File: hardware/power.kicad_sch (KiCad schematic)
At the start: 12 parts, among them J18 Power, SW7 POWER, U14 NCP1117-5.0_SOT223, U15 B0505S-1WR3

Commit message: Reset references and remove THT footprint assignments.
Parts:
- removed J18: Power, Connector_BarrelJack:BarrelJack_Horizontal, symbol Connector:Barrel_Jack_Switch
- added J19: DC, symbol Connector_Generic:Conn_01x03
- D8: footprint Diode_THT:D_DO-41_SOD81_P2.54mm_Vertical_AnodeUp -> (none)
- renumbered R64 to R70, SW7 to SW6
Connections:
- net GND: now also J19.3 (Pin_3)
- net at SW6.1 (A): now also J19.1 (Pin_1)
- net at BT1.1 (+): now also J19.2 (Pin_2)
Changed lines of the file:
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@@
-	)
-	(symbol
-		(lib_id "Connector:Barrel_Jack_Switch")
-		(at 35.56 91.44 0)
-		(mirror x)
-		(unit 1)
-		(exclude_from_sim no)
-		(in_bom yes)
-		(on_board yes)
-		(dnp no)
-		(property "Reference" "J18"
-			(at 35.56 82.55 0)
-			(effects
-				(font
-					(size 1.27 1.27)
-				)
-			)
-		)
-		(property "Value" "Power"
-			(at 35.56 85.0869 0)
-			(effects
-				(font
-					(size 1.27 1.27)
-				)
-			)
-		)
-		(property "Footprint" "Connector_BarrelJack:BarrelJack_Horizontal"
-			(at 36.83 90.424 0)
-			(effects
-				(font
-					(size 1.27 1.27)
-				)
-				(hide yes)
-			)
-		)
-		(property "Datasheet" "~"
-			(at 36.83 90.424 0)
-			(effects
-				(font
-					(size 1.27 1.27)
-				)
-				(hide yes)
-			)
-		)
-		(property "Description" "DC Barrel Jack with an internal switch"
-			(at 35.56 91.44 0)
-			(effects
-				(font
-					(size 1.27 1.27)
-				)
-				(hide yes)
-			)
-		)
-		(pin "1"
-		)
-		(pin "2"
-		)
-		(pin "3"
-		)
-		(instances
-			(project "Zero-Stomp"
-				(path "/8c8d5801-9c58-4283-98ac-c6a8e7250e15/19d3dfe6-4a06-4dc4-92a9-6134eae12961"
-					(reference "J18")
-					(unit 1)
-				)
-			)
-		)
 	)
 	(symbol
@@
 		(dnp no)
 		(fields_autoplaced yes)
-		(property "Reference" "SW7"
+		(property "Reference" "SW6"
 			(at 64.77 82.55 0)
 			(effects
@@
 			(project ""
 				(path "/8c8d5801-9c58-4283-98ac-c6a8e7250e15/19d3dfe6-4a06-4dc4-92a9-6134eae12961"
-					(reference "SW7")
+					(reference "SW6")
 					(unit 1)
 				)
@@
 		(on_board yes)
 		(dnp no)
-		(property "Reference" "R64"
+		(property "Reference" "R70"
 			(at 147.32 92.71 90)
 			(effects
@@
 			(project "Zero-Stomp"
 				(path "/8c8d5801-9c58-4283-98ac-c6a8e7250e15/19d3dfe6-4a06-4dc4-92a9-6134eae12961"
-					(reference "R64")
+					(reference "R70")
 					(unit 1)
 				)
@@
 			)
 		)
-		(property "Footprint" "Diode_THT:D_DO-41_SOD81_P2.54mm_Vertical_AnodeUp"
+		(property "Footprint" ""
 			(at 138.43 81.915 0)
 			(effects
@@
 					(unit 1)
 				)
+			)
+		)
+	)
+	(symbol
+		(lib_id "Connector_Generic:Conn_01x03")
+		(at 38.1 91.44 0)
+		(mirror y)
+		(unit 1)
+		(exclude_from_sim no)
+		(in_bom yes)
+		(on_board yes)
+		(dnp no)
+		(fields_autoplaced yes)
+		(property "Reference" "J19"
+			(at 38.1 82.55 0)
+			(effects
+				(font
+					(size 1.27 1.27)
+				)
+			)
+		)
+		(property "Value" "DC"
+			(at 38.1 85.09 0)
+			(effects
+				(font
+					(size 1.27 1.27)
+				)
+			)
+		)
+		(property "Footprint" ""
+			(at 38.1 91.44 0)
+			(effects
+				(font
+					(size 1.27 1.27)
+				)
+				(hide yes)
+			)
+		)
+		(property "Datasheet" "~"
+			(at 38.1 91.44 0)
+			(effects
+				(font
+					(size 1.27 1.27)
+				)
+				(hide yes)
+			)
+		)
+		(property "Description" "Generic connector, single row, 01x03, script generated (kicad-library-utils/schlib/autogen/connector/)"
+			(at 38.1 91.44 0)
+			(effects
+				(font
+					(size 1.27 1.27)
+				)
+				(hide yes)
+			)
+		)
+		(pin "1"
+		)
+		(pin "3"
+		)
+		(pin "2"
+		)
+		(instances
+			(project ""
+				(path "/8c8d5801-9c58-4283-98ac-c6a8e7250e15/19d3dfe6-4a06-4dc4-92a9-6134eae12961"
+					(reference "J19")
+					(unit 1)
+				)

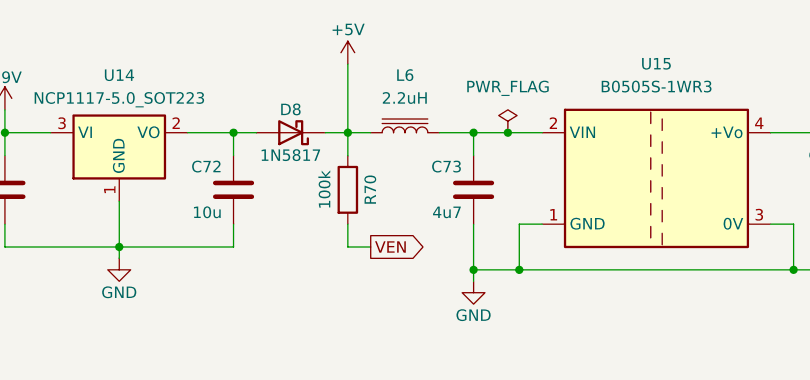
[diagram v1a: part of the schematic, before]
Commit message: Footprint assignments
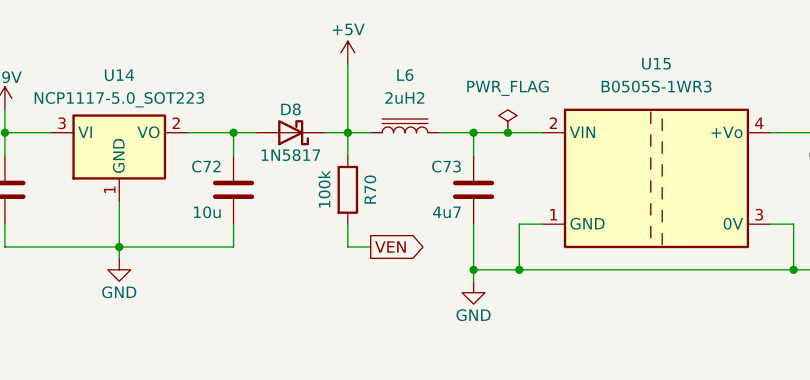
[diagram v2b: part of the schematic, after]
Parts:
- C71, C72, C74: footprint (none) -> Capacitor_SMD:C_0805_2012Metric
- C73: footprint (none) -> Capacitor_SMD:C_0603_1608Metric
- D8: footprint (none) -> Diode_SMD:D_SOD-123
- J19: footprint (none) -> Connector_JST:JST_PH_B3B-PH-K_1x03_P2.00mm_Vertical
- L6: value 2.2uH -> 2uH2; footprint (none) -> Inductor_SMD:L_12x12mm_H4.5mm
- R70: footprint (none) -> Resistor_SMD:R_0603_1608Metric
- SW6: footprint (none) -> Connector_JST:JST_PH_B2B-PH-K_1x02_P2.00mm_Vertical
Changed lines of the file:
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@@
 			)
 		)
-		(property "Footprint" ""
+		(property "Footprint" "Capacitor_SMD:C_0805_2012Metric"
 			(at 131.1148 96.52 0)
 			(effects
@@
 			)
 		)
-		(property "Footprint" ""
+		(property "Footprint" "Connector_JST:JST_PH_B2B-PH-K_1x02_P2.00mm_Vertical"
 			(at 64.77 88.9 0)
 			(effects
@@
 			)
 		)
-		(property "Footprint" ""
+		(property "Footprint" "Resistor_SMD:R_0603_1608Metric"
 			(at 143.002 92.71 90)
 			(effects
@@
 			)
 		)
-		(property "Footprint" ""
+		(property "Footprint" "Capacitor_SMD:C_0603_1608Metric"
 			(at 157.7848 96.52 0)
 			(effects
@@
 			)
 		)
-		(property "Value" "2.2uH"
+		(property "Value" "2uH2"
 			(at 151.13 82.55 90)
 			(effects
@@
 			)
 		)
-		(property "Footprint" ""
+		(property "Footprint" "Inductor_SMD:L_12x12mm_H4.5mm"
 			(at 151.13 86.36 0)
 			(effects
@@
 			)
 		)
-		(property "Footprint" ""
+		(property "Footprint" "Capacitor_SMD:C_0805_2012Metric"
 			(at 199.6948 95.25 0)
 			(effects
@@
 			)
 		)
-		(property "Footprint" ""
+		(property "Footprint" "Diode_SMD:D_SOD-123"
 			(at 138.43 81.915 0)
 			(effects
@@
 			)
 		)
-		(property "Footprint" ""
+		(property "Footprint" "Capacitor_SMD:C_0805_2012Metric"
 			(at 105.7148 96.52 0)
 			(effects
@@
 			)
 		)
-		(property "Footprint" ""
+		(property "Footprint" "Connector_JST:JST_PH_B3B-PH-K_1x03_P2.00mm_Vertical"
 			(at 38.1 91.44 0)
 			(effects

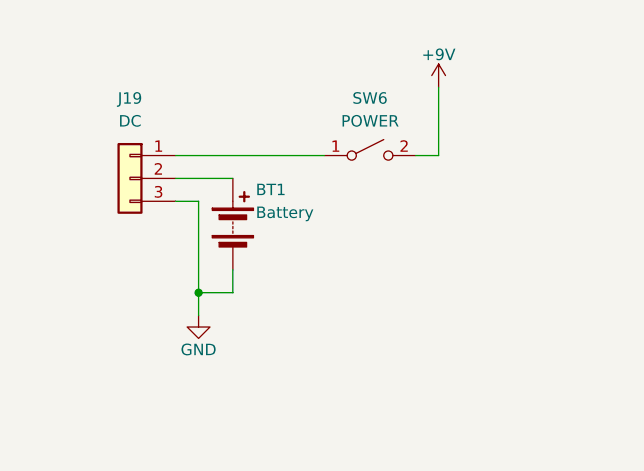
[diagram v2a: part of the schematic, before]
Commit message: Add power switch and bypass jumper
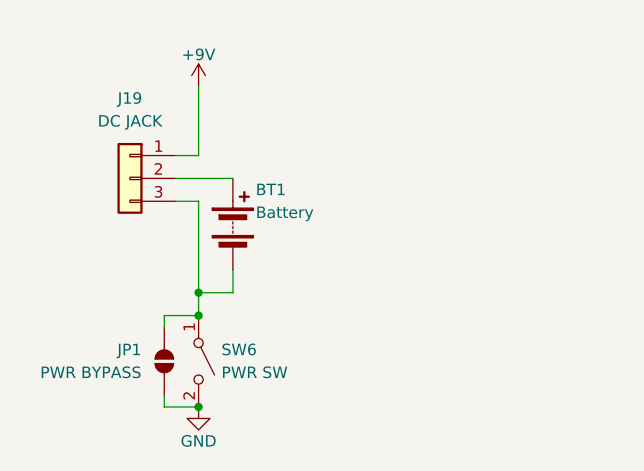
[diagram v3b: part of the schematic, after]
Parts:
- added JP1: PWR BYPASS, Jumper:SolderJumper-2_P1.3mm_Open_RoundedPad1.0x1.5mm, symbol Jumper:SolderJumper_2_Open
- J19: value DC -> DC JACK; footprint Connector_JST:JST_PH_B3B-PH-K_1x03_P2.00mm_Vertical -> Connector_JST:JST_PH_S3B-PH-K_1x03_P2.00mm_Horizontal
- L6: footprint Inductor_SMD:L_12x12mm_H4.5mm -> Inductor_SMD:L_Sunlord_SWPA3015S
- SW6: value POWER -> PWR SW; footprint Connector_JST:JST_PH_B2B-PH-K_1x02_P2.00mm_Vertical -> Connector_JST:JST_SH_SM02B-SRSS-TB_1x02-1MP_P1.00mm_Horizontal
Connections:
- net +9V: now also J19.1 (Pin_1); no longer SW6.2 (B)
- net GND: now also SW6.2 (B), JP1.1 (A); no longer BT1.2 (-), J19.3 (Pin_3)
- net at SW6.1 (A): now also BT1.2 (-), J19.3 (Pin_3), JP1.2 (B); no longer J19.1 (Pin_1)
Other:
- moved on the sheet: SW6
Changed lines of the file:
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@@
+	)
+	(junction
+		(at 45.72 106.68)
+		(diameter 0)
+		(color 0 0 0 0)
 	)
 	(junction
@@
 	)
 	(junction
+		(at 45.72 116.84)
+		(diameter 0)
+		(color 0 0 0 0)
+	)
+	(junction
 		(at 144.78 86.36)
 		(diameter 0)
@@
 	(wire
 		(pts
+			(xy 41.91 106.68) (xy 45.72 106.68)
+		)
+		(stroke
+			(width 0)
+			(type default)
+		)
+	)
+	(wire
+		(pts
 			(xy 163.83 101.6) (xy 163.83 96.52)
 		)
@@
 	(wire
 		(pts
+			(xy 41.91 116.84) (xy 45.72 116.84)
+		)
+		(stroke
+			(width 0)
+			(type default)
+		)
+	)
+	(wire
+		(pts
 			(xy 163.83 101.6) (xy 194.31 101.6)
 		)
@@
 	(wire
 		(pts
+			(xy 41.91 115.57) (xy 41.91 116.84)
+		)
+		(stroke
+			(width 0)
+			(type default)
+		)
+	)
+	(wire
+		(pts
 			(xy 106.68 99.06) (xy 119.38 99.06)
 		)
@@
 	(wire
 		(pts
-			(xy 72.39 88.9) (xy 69.85 88.9)
+			(xy 45.72 88.9) (xy 43.18 88.9)
 		)
 		(stroke
@@
 	(wire
 		(pts
-			(xy 72.39 81.28) (xy 72.39 88.9)
+			(xy 45.72 81.28) (xy 45.72 88.9)
 		)
 		(stroke
@@
 	(wire
 		(pts
+			(xy 41.91 107.95) (xy 41.91 106.68)
+		)
+		(stroke
+			(width 0)
+			(type default)
+		)
+	)
+	(wire
+		(pts
 			(xy 45.72 93.98) (xy 45.72 104.14)
 		)
@@
 		(pts
 			(xy 191.77 86.36) (xy 200.66 86.36)
-		)
-		(stroke
-			(width 0)
-			(type default)
-		)
-	)
-	(wire
-		(pts
-			(xy 43.18 88.9) (xy 59.69 88.9)
 		)
 		(stroke
@@
 	(symbol
 		(lib_id "power:+9V")
-		(at 72.39 81.28 0)
+		(at 45.72 81.28 0)
 		(unit 1)
 		(exclude_from_sim no)
@@
 		(fields_autoplaced yes)
 		(property "Reference" "#PWR0104"
-			(at 72.39 85.09 0)
+			(at 45.72 85.09 0)
 			(effects
 				(font
@@
 		)
 		(property "Value" "+9V"
-			(at 72.39 77.7042 0)
+			(at 45.72 77.7042 0)
 			(effects
 				(font
@@
 		)
 		(property "Footprint" ""
-			(at 72.39 81.28 0)
+			(at 45.72 81.28 0)
 			(effects
 				(font
@@
 		)
 		(property "Datasheet" ""
-			(at 72.39 81.28 0)
+			(at 45.72 81.28 0)
 			(effects
 				(font
@@
 		)
 		(property "Description" "Power symbol creates a global label with name \"+9V\""
-			(at 72.39 81.28 0)
+			(at 45.72 81.28 0)
 			(effects
 				(font
@@
 	(symbol
 		(lib_id "Switch:SW_SPST")
-		(at 64.77 88.9 0)
+		(at 45.72 111.76 270)
 		(unit 1)
 		(exclude_from_sim no)
@@
 		(fields_autoplaced yes)
 		(property "Reference" "SW6"
-			(at 64.77 82.55 0)
-			(effects
-				(font
-					(size 1.27 1.27)
-				)
-			)
-		)
-		(property "Value" "POWER"
-			(at 64.77 85.09 0)
-			(effects
-				(font
-					(size 1.27 1.27)
-				)
-			)
-		)
-		(property "Footprint" "Connector_JST:JST_PH_B2B-PH-K_1x02_P2.00mm_Vertical"
-			(at 64.77 88.9 0)
+			(at 48.26 110.4899 90)
+			(effects
+				(font
+					(size 1.27 1.27)
+				)
+				(justify left)
+			)
+		)
+		(property "Value" "PWR SW"
+			(at 48.26 113.0299 90)
+			(effects
+				(font
+					(size 1.27 1.27)
+				)
+				(justify left)
+			)
+		)
+		(property "Footprint" "Connector_JST:JST_SH_SM02B-SRSS-TB_1x02-1MP_P1.00mm_Horizontal"
+			(at 45.72 111.76 0)
 			(effects
 				(font
@@
 		)
 		(property "Datasheet" "~"
-			(at 64.77 88.9 0)
+			(at 45.72 111.76 0)
 			(effects
 				(font
@@
 		)
 		(property "Description" "Single Pole Single Throw (SPST) switch"
-			(at 64.77 88.9 0)
+			(at 45.72 111.76 0)
 			(effects
 				(font
@@
 		)
 		(instances
-			(project ""
+			(project "Zero-Stomp"
 				(path "/8c8d5801-9c58-4283-98ac-c6a8e7250e15/19d3dfe6-4a06-4dc4-92a9-6134eae12961"
 					(reference "SW6")
@@
 			)
 		)
-		(property "Footprint" "Inductor_SMD:L_12x12mm_H4.5mm"
+		(property "Footprint" "Inductor_SMD:L_Sunlord_SWPA3015S"
 			(at 151.13 86.36 0)
 			(effects
@@
 			)
 		)
-		(property "Value" "DC"
+		(property "Value" "DC JACK"
 			(at 38.1 85.09 0)
 			(effects
@@
 			)
 		)
-		(property "Footprint" "Connector_JST:JST_PH_B3B-PH-K_1x03_P2.00mm_Vertical"
+		(property "Footprint" "Connector_JST:JST_PH_S3B-PH-K_1x03_P2.00mm_Horizontal"
 			(at 38.1 91.44 0)
 			(effects
@@
 	(symbol
 		(lib_id "power:GND")
-		(at 45.72 106.68 0)
+		(at 45.72 116.84 0)
 		(unit 1)
 		(exclude_from_sim no)
@@
 		(dnp no)
 		(property "Reference" "#PWR0103"
-			(at 45.72 113.03 0)
+			(at 45.72 123.19 0)
 			(effects
 				(font
@@
 		)
 		(property "Value" "GND"
-			(at 45.72 110.49 0)
+			(at 45.72 120.65 0)
 			(effects
 				(font
@@
 		)
 		(property "Footprint" ""
-			(at 45.72 106.68 0)
+			(at 45.72 116.84 0)
 			(effects
 				(font
@@
 		)
 		(property "Datasheet" ""
-			(at 45.72 106.68 0)
+			(at 45.72 116.84 0)
 			(effects
 				(font
@@
 		)
 		(property "Description" "Power symbol creates a global label with name \"GND\" , ground"
-			(at 45.72 106.68 0)
+			(at 45.72 116.84 0)
 			(effects
 				(font
@@
 					(unit 1)
 				)
+			)
+		)
+	)
+	(symbol
+		(lib_id "Jumper:SolderJumper_2_Open")
+		(at 41.91 111.76 90)
+		(unit 1)
+		(exclude_from_sim no)
+		(in_bom no)
+		(on_board yes)
+		(dnp no)
+		(property "Reference" "JP1"
+			(at 39.37 110.4899 90)
+			(effects
+				(font
+					(size 1.27 1.27)
+				)
+				(justify left)
+			)
+		)
+		(property "Value" "PWR BYPASS"
+			(at 39.37 113.0299 90)
+			(effects
+				(font
+					(size 1.27 1.27)
+				)
+				(justify left)
+			)
+		)
+		(property "Footprint" "Jumper:SolderJumper-2_P1.3mm_Open_RoundedPad1.0x1.5mm"
+			(at 41.91 111.76 0)
+			(effects
+				(font
+					(size 1.27 1.27)
+				)
+				(hide yes)
+			)
+		)
+		(property "Datasheet" "~"
+			(at 41.91 111.76 0)
+			(effects
+				(font
+					(size 1.27 1.27)
+				)
+				(hide yes)
+			)
+		)
+		(property "Description" "Solder Jumper, 2-pole, open"
+			(at 41.91 111.76 0)
+			(effects
+				(font
+					(size 1.27 1.27)
+				)
+				(hide yes)
+			)
+		)
+		(pin "1"
+		)
+		(pin "2"
+		)
+		(instances
+			(project ""
+				(path "/8c8d5801-9c58-4283-98ac-c6a8e7250e15/19d3dfe6-4a06-4dc4-92a9-6134eae12961"
+					(reference "JP1")
+					(unit 1)
+				)
